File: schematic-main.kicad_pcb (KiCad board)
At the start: 2 copper layers, 87 x 72.4 mm, 73 parts, among them J1 Conn_01x02, J2 Conn_01x03, J3 Conn_01x02, J6 Conn_01x04, P1 USB_C_Plug_USB2.0, U1 LM76202-Q1, U2 TPS62933, U3 USBLC6-2P6, U4 ESP32-S3FN8, U5 SN65HVD232, U6 PC817, U7 PC817, Y1 Crystal_GND24

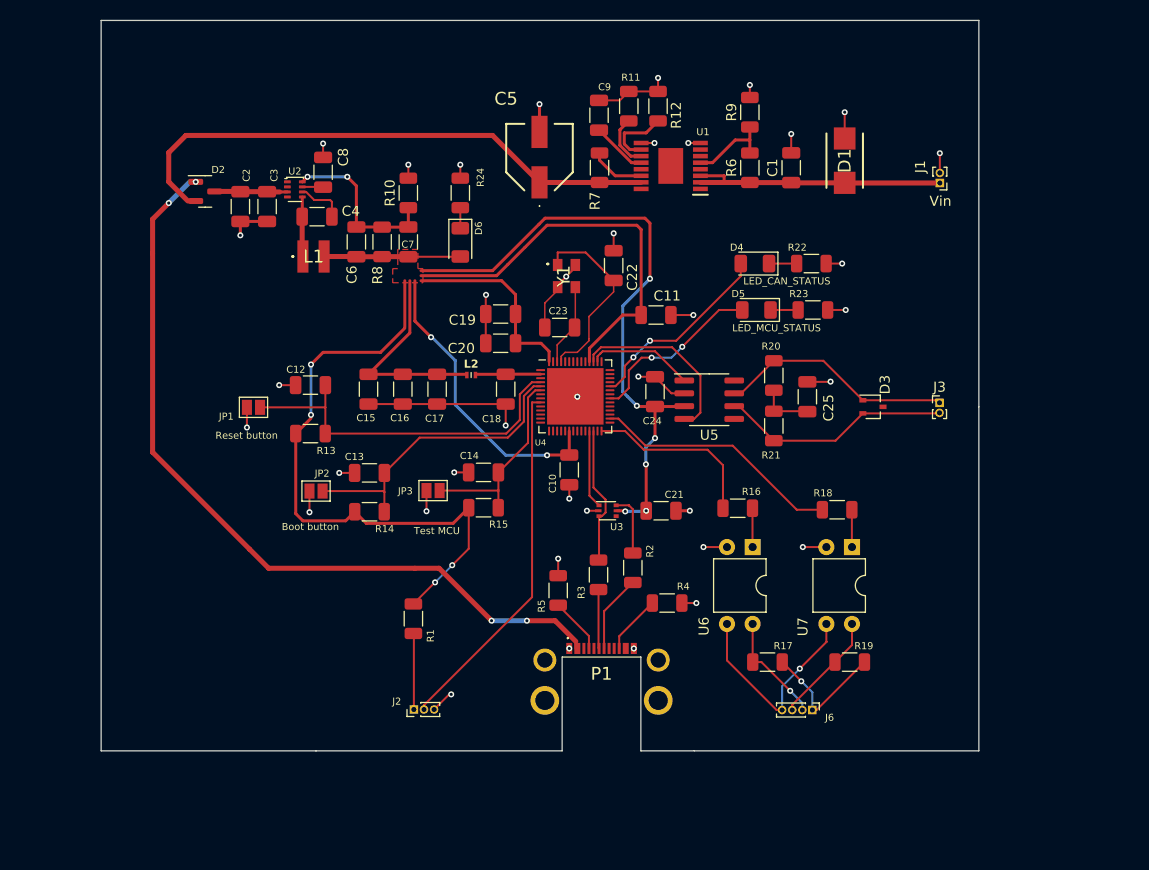
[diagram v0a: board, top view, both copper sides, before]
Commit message: Add Molex, change of layout for CAN and Optocouplers
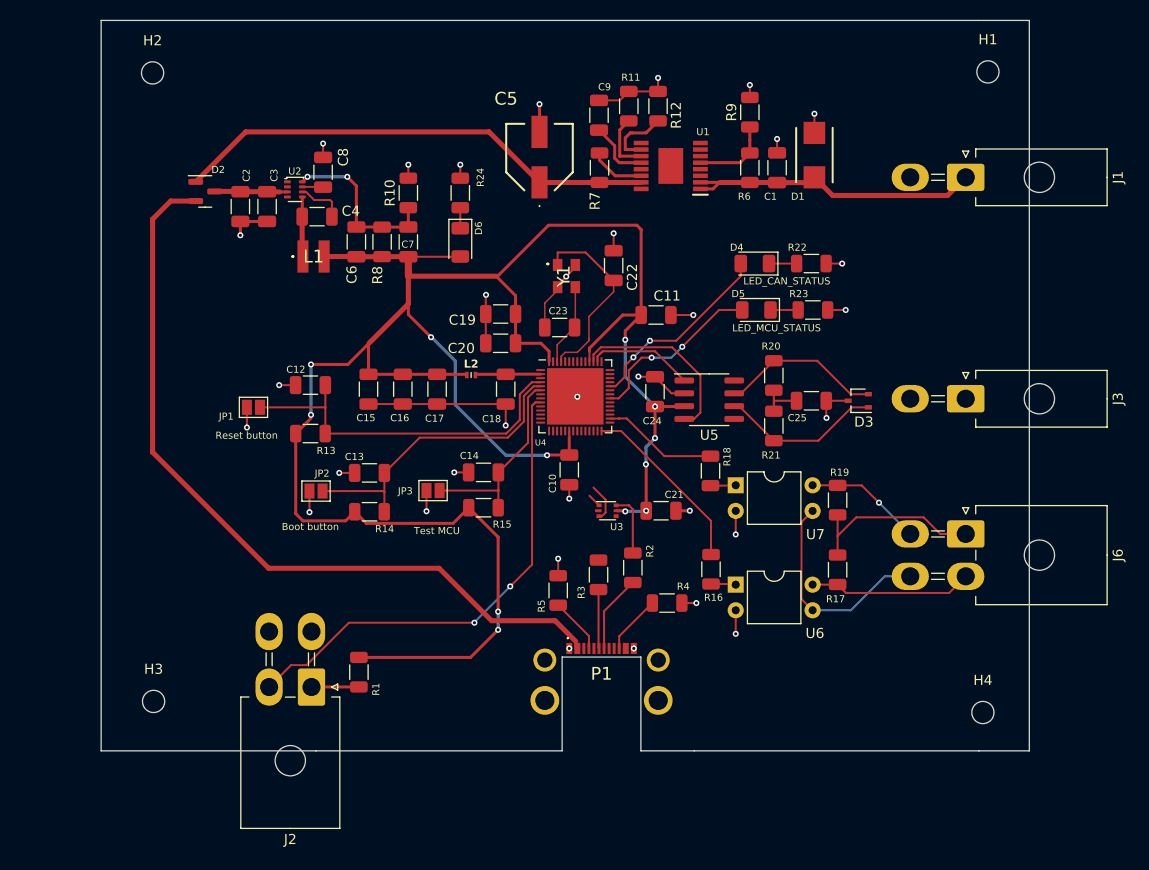
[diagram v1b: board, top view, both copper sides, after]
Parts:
- added H1: MountingHole, MountingHole:MountingHole_2.2mm_M2, F.Cu at (141.9, 56.8)
- added H2: MountingHole, MountingHole:MountingHole_2.2mm_M2, F.Cu at (59.1, 56.9)
- added H3: MountingHole, MountingHole:MountingHole_2.2mm_M2, F.Cu at (59.2, 119.2)
- added H4: MountingHole, MountingHole:MountingHole_2.2mm_M2, F.Cu at (141.4, 120.3)
- J1, J3: footprint Connector_PinHeader_1.00mm:PinHeader_1x02_P1.00mm_Vertical -> Connector_Molex:Molex_Mini-Fit_Jr_5569-02A2_2x01_P4.20mm_Horizontal
- J2: footprint Connector_PinHeader_1.00mm:PinHeader_1x03_P1.00mm_Vertical -> Connector_Molex:Molex_Mini-Fit_Jr_5569-04A2_2x02_P4.20mm_Horizontal
- J6: footprint Connector_PinHeader_1.00mm:PinHeader_1x04_P1.00mm_Vertical -> Connector_Molex:Molex_Mini-Fit_Jr_5569-04A2_2x02_P4.20mm_Horizontal
- moved J6 23.1 mm to (139.7, 102.6)
- moved R19 16.1 mm to (127.0, 99.2), turned to 90 degrees
- moved R18 13.1 mm to (114.4, 96.3), turned to -90 degrees
- moved U7 13.1 mm to (116.9, 97.8), turned to 0 degrees
- moved R17 11.5 mm to (127.0, 106.2), turned to -90 degrees
- moved J2 10.4 mm to (74.8, 117.8), turned to 180 degrees
- moved R1 7.57 mm to (79.5, 116.3)
- moved R16 6.60 mm to (114.5, 106.1), turned to -90 degrees
- moved U6 4.08 mm to (116.9, 107.6), turned to 0 degrees
- moved D1 3.05 mm to (124.7, 65.0)
- moved J3 2.63 mm to (139.7, 89.2), turned to -90 degrees
- moved J1 2.63 mm to (139.7, 67.2), turned to -90 degrees
- moved D3 1.57 mm to (129.1, 89.4), turned to 180 degrees
- moved C1 1.40 mm to (121.0, 66.3)
- moved C25 0.57 mm to (124.4, 89.4), turned to 0 degrees
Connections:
- D2 pad 1: /VBUS -> /Power /Vreg
- D2 pad 2: /Power /Vreg -> /VBUS
- D3 pad 1: /IO/CANH -> /IO/CANL
- D3 pad 2: /IO/CANL -> /IO/CANH
- U1 pad 2: /Power /Vin -> (no net)
- U1 pad 3: /Power /Vin -> (no net)
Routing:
- net +3.3V: track 249.1 -> 215.4 mm
- net /IO/MOTOR_ON_OFF_MCU: track 24.8 -> 11.5 mm
- net /MCU/SPEED_OUTPUT: track 35.7 -> 47.9 mm, vias 0 -> 2
- net /MCU/USB_D+: track 13.7 -> 3.84 mm
- net /Power /Vreg: track 55.8 -> 48.3 mm
- net /IO/CANH: track 23.4 -> 16.0 mm
- net /IO/CANL: track 22.9 -> 16.1 mm
- net /MCU/USB_D-: track 13.9 -> 7.50 mm
- net /PWM_MOTOR: track 11.1 -> 16.2 mm, vias 1 -> 0
- net GND: track 93.9 -> 88.9 mm, vias 36 -> 33
- net /IO/5V_MOTOR: track 13.1 -> 18.1 mm, vias 1 -> 0
- net /Power /Vin: track 26.8 -> 30.3 mm
- net Net-(J2-Pin_1): track 7.56 -> 4.71 mm
- net (no net): track 2.53 -> 0.00 mm, vias 2 -> 0
- net Net-(R18-Pad2): track 3.71 -> 2.52 mm
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- removed copper zone on F.Cu, net +3.3V
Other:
- board size 87 x 72.4 mm -> 92 x 72.4 mm
- board text removed: "Vin"

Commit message: Changing footprints for capacitors C >= 10 uF
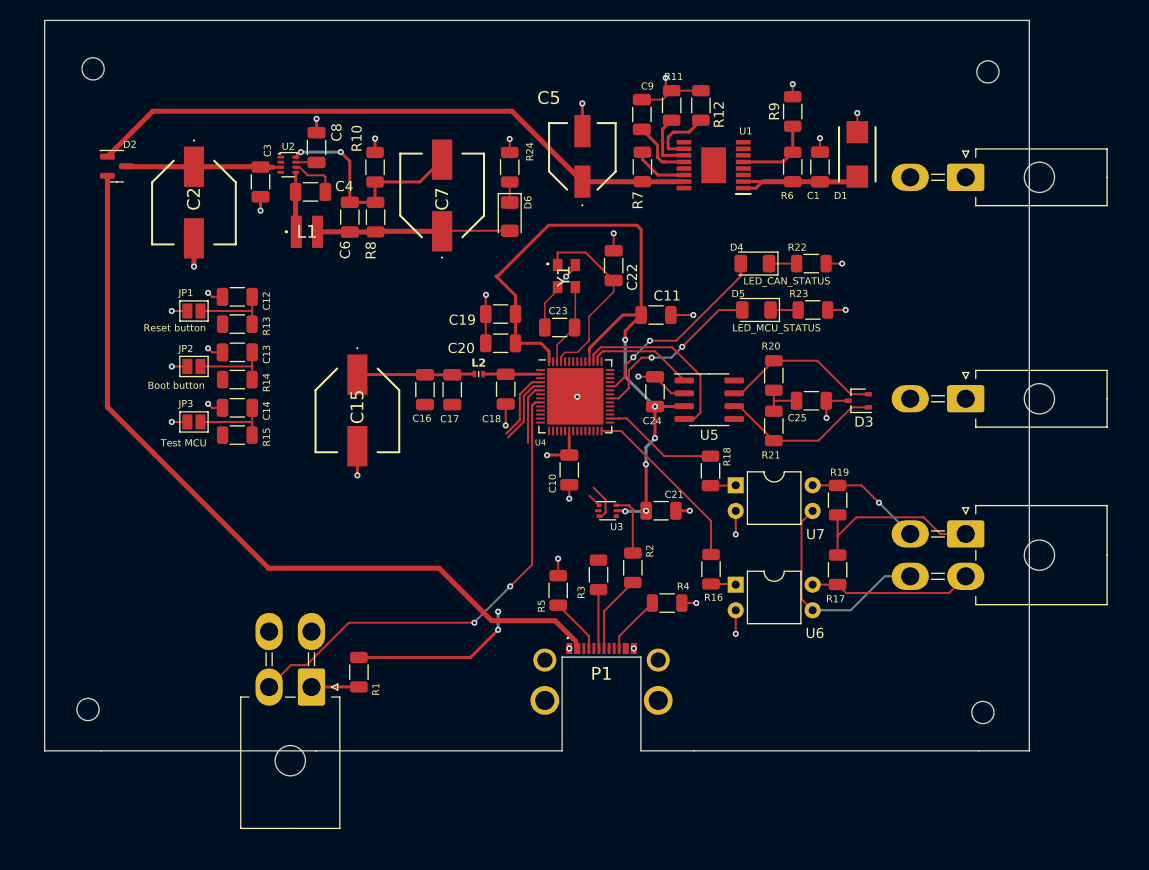
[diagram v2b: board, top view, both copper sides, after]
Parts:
- C15, C2, C7: footprint Capacitor_SMD:C_1206_3216Metric -> Capacitor_Tantalum_SMD:EEHZT1E331UP
- moved R15 25.4 mm to (67.5, 92.8)
- moved C14 25.2 mm to (67.5, 90.1)
- moved JP3 24.7 mm to (63.2, 91.5)
- moved R14 18.5 mm to (67.5, 87.3)
- moved C13 17.7 mm to (67.5, 84.6)
- moved JP2 17.3 mm to (63.2, 86.0)
- moved R13 13.0 mm to (67.5, 81.8)
- moved C12 11.4 mm to (67.5, 79.1)
- moved JP1 11.2 mm to (63.2, 80.5)
- moved D2 9.10 mm to (55.6, 66.2)
- moved H3 6.55 mm to (52.7, 120.0)
- moved H2 5.91 mm to (53.2, 56.5)
- moved C7 5.69 mm to (87.8, 69.0)
- moved D6 5.52 mm to (94.5, 71.2)
- moved R24 5.52 mm to (94.5, 66.2)
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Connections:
- U1 pad 15: /Power /Vreg -> (no net)
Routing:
- net +3.3V: track 215.4 -> 124.9 mm, vias 12 -> 9
- net /MCU/RESET: track 36.2 -> 14.8 mm
- net /Power /Vin: track 30.3 -> 13.8 mm
- net /MCU/BOOT: track 30.6 -> 14.7 mm
- net /Power /Vreg: track 48.3 -> 61.9 mm
- net GND: track 88.9 -> 77.1 mm, vias 33 -> 35
- net Net-(U2-VIN): track 7.27 -> 15.4 mm
- net /MCU/MCU_TEST: track 19.5 -> 13.8 mm
- net Net-(U2-FB): track 17.1 -> 22.2 mm
- net /VBUS: track 78.5 -> 79.9 mm
- net VDD3P3: track 6.78 -> 6.01 mm
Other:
- board size 92 x 72.4 mm -> 97.6 x 72.4 mm

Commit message: Adding library and fixing errors related to the ideal diode
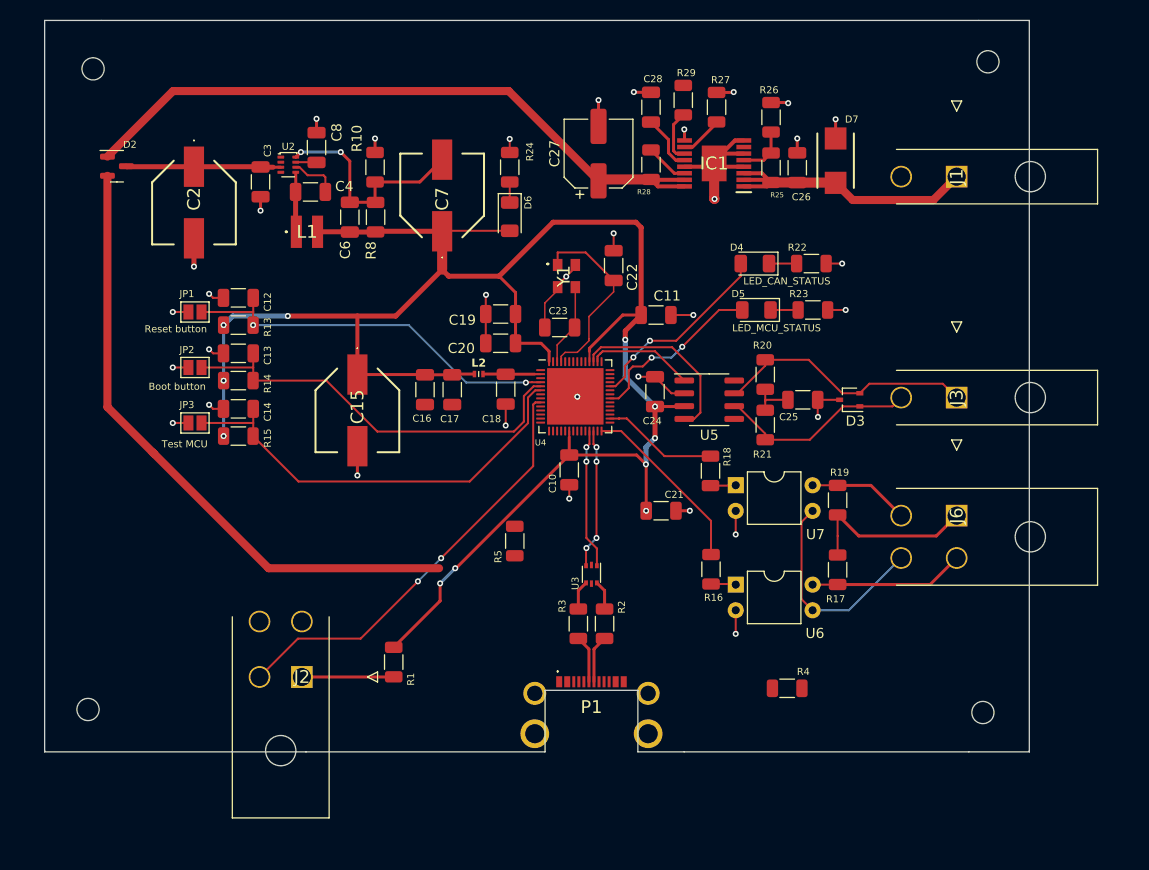
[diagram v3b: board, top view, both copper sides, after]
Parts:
- removed C1: 1u, Capacitor_SMD:C_1206_3216Metric
- removed C5: 47u, Capacitor_Tantalum_SMD:EEE0JA331XP
- removed C9: 2n7, Capacitor_SMD:C_1206_3216Metric
- removed D1: TPSMC30CA, Diode_SMD:DIONM5436X244N
- removed R11: 56k, Resistor_SMD:R_1206_3216Metric
- removed R12, R7: 100k, Resistor_SMD:R_1206_3216Metric
- removed R6: 180k, Resistor_SMD:R_1206_3216Metric
- removed R9: 12k, Resistor_SMD:R_1206_3216Metric
- removed U1: LM76202-Q1, Diode_SMD:SOP65P640X120-17N
- added C26: 1u, Capacitor_SMD:C_1206_3216Metric, F.Cu at (123.0, 66.3)
- added C27: 47u, Capacitor_SMD:CP_Elec_6.3x7.7, F.Cu at (103.3, 64.9)
- added C28: 2n7, Capacitor_SMD:C_1206_3216Metric, F.Cu at (108.5, 60.3)
- added D7: TPSMC30CA, Diode_SMD:DIONM5436X244N, F.Cu at (126.8, 65.6)
- added IC1: LM76202QPWPRQ1, Diode_SMD:SOP65P640X120-17N, F.Cu at (114.8, 65.9)
- added R25: 180k, Resistor_SMD:R_1206_3216Metric, F.Cu at (120.4, 66.3)
- added R26: 12k, Resistor_SMD:R_1206_3216Metric, F.Cu at (120.4, 61.3)
- added R27: 100k, Resistor_SMD:R_1206_3216Metric, F.Cu at (115.0, 60.3)
- added R28: 100k, Resistor_SMD:R_1206_3216Metric, F.Cu at (108.5, 66.0)
- added R29: 56k, Resistor_SMD:R_1206_3216Metric, F.Cu at (111.7, 59.6)
- J1, J3: footprint Connector_Molex:Molex_Mini-Fit_Jr_5569-02A2_2x01_P4.20mm_Horizontal -> Connector_Molex:39-30-102Y
- J2, J6: footprint Connector_Molex:Molex_Mini-Fit_Jr_5569-04A2_2x02_P4.20mm_Horizontal -> Connector_Molex:39-30-104Y
- moved R4 14.6 mm to (122.0, 117.9)
- moved R5 6.52 mm to (95.0, 103.3)
- moved U3 6.50 mm to (102.6, 106.6), turned to -90 degrees
- moved R2 6.22 mm to (103.9, 111.5)
- moved R3 5.25 mm to (101.3, 111.5)
- moved R1 3.59 mm to (83.0, 115.3)
- moved P1 3.45 mm to (102.6, 120.1)
- moved J6 2.03 mm to (138.8, 100.8), turned to 90 degrees
- moved J2 1.38 mm to (73.9, 116.8), turned to 0 degrees
- moved H1 1.00 mm to (141.9, 55.8)
- moved J3 0.91 mm to (138.8, 89.1), turned to 90 degrees
- moved J1 0.90 mm to (138.8, 67.2), turned to 90 degrees
- moved D3 0.86 mm to (128.2, 89.3)
- moved C25 0.86 mm to (123.5, 89.3)
- moved R20 0.86 mm to (119.8, 86.8)
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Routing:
- net +3.3V: track 124.9 -> 187.8 mm, vias 9 -> 11
- net /MCU/MCU_TEST: track 13.8 -> 43.4 mm
- net /MCU/BOOT: track 14.7 -> 41.8 mm
- net /MCU/RESET: track 14.8 -> 38.7 mm, vias 0 -> 2
- net /VBUS: track 79.9 -> 62.7 mm
- net /Power /Vin: track 13.8 -> 28.8 mm
- net /MCU/USB_D+: track 3.84 -> 16.8 mm, vias 0 -> 4
- net GND: track 77.1 -> 88.3 mm, vias 35 -> 34
- net /IO/CANH: track 16.0 -> 26.1 mm
- net /MCU/USB_D-: track 7.50 -> 16.8 mm, vias 0 -> 2
- net Net-(U1-OVP): track 7.87 -> 0.00 mm
- net Net-(U1-IMON): track 6.67 -> 0.00 mm
- net Net-(U1-dVdT): track 6.23 -> 0.00 mm
- net Net-(U1-ILIM): track 5.98 -> 0.00 mm
- net Net-(P1-VCONN): track 5.86 -> 0.00 mm
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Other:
- board size 97.6 x 72.4 mm -> 97.6 x 72.5 mm

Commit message: Adding filled areas and seting USB
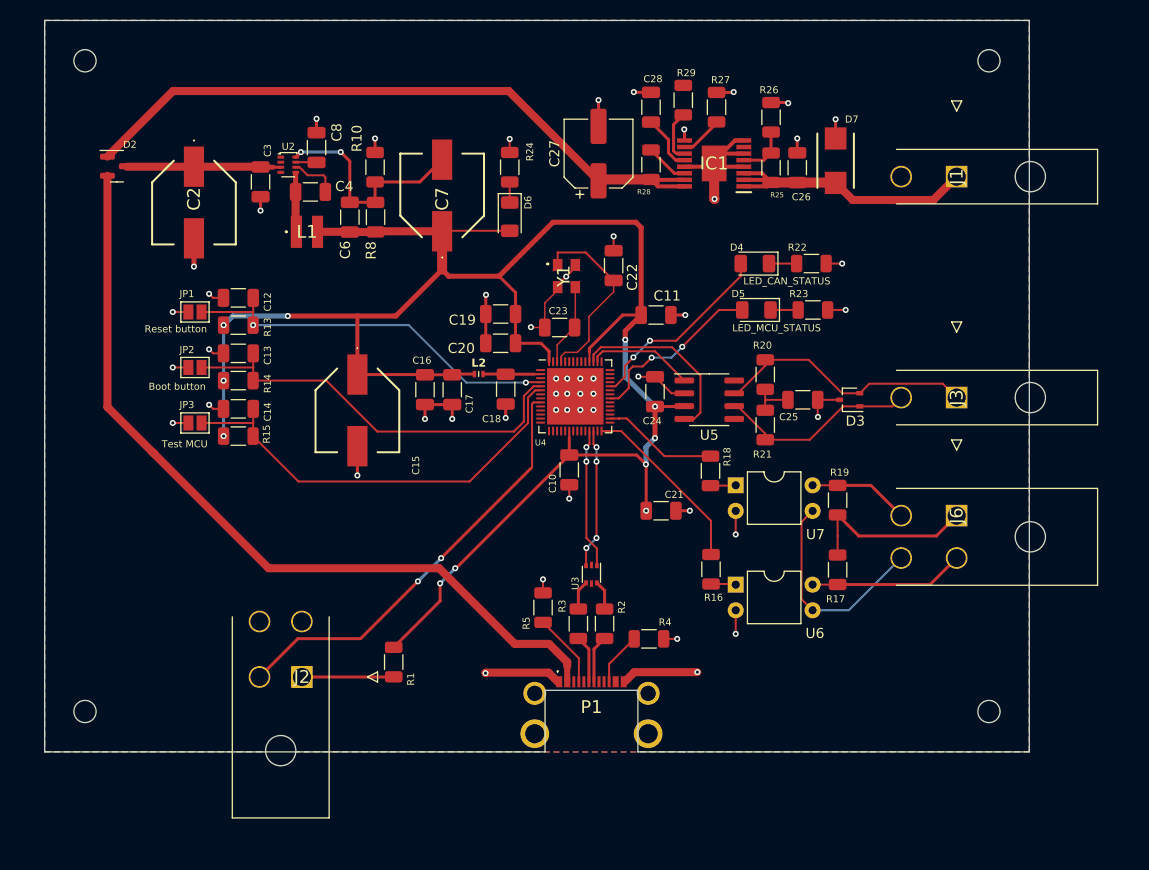
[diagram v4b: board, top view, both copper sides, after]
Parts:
- moved R4 14.5 mm to (108.3, 113.0)
- moved R5 7.17 mm to (97.8, 109.9)
- moved H2 1.13 mm to (52.4, 55.7)
- moved H4 0.61 mm to (142.0, 120.2)
- moved H3 0.36 mm to (52.4, 120.2)
- moved H1 0.14 mm to (142.0, 55.7)
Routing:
- net GND: track 88.3 -> 111.2 mm, vias 34 -> 52
- net /VBUS: track 62.7 -> 82.8 mm
- net Net-(P1-CC): track 0.00 -> 7.36 mm
- net Net-(P1-VCONN): track 0.00 -> 5.28 mm
- added copper zone on B.Cu, net GND
- added copper zone on F.Cu, net GND

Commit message: Changing placements of SolderJumper, CAN connector to 3 pins, traces 0,4
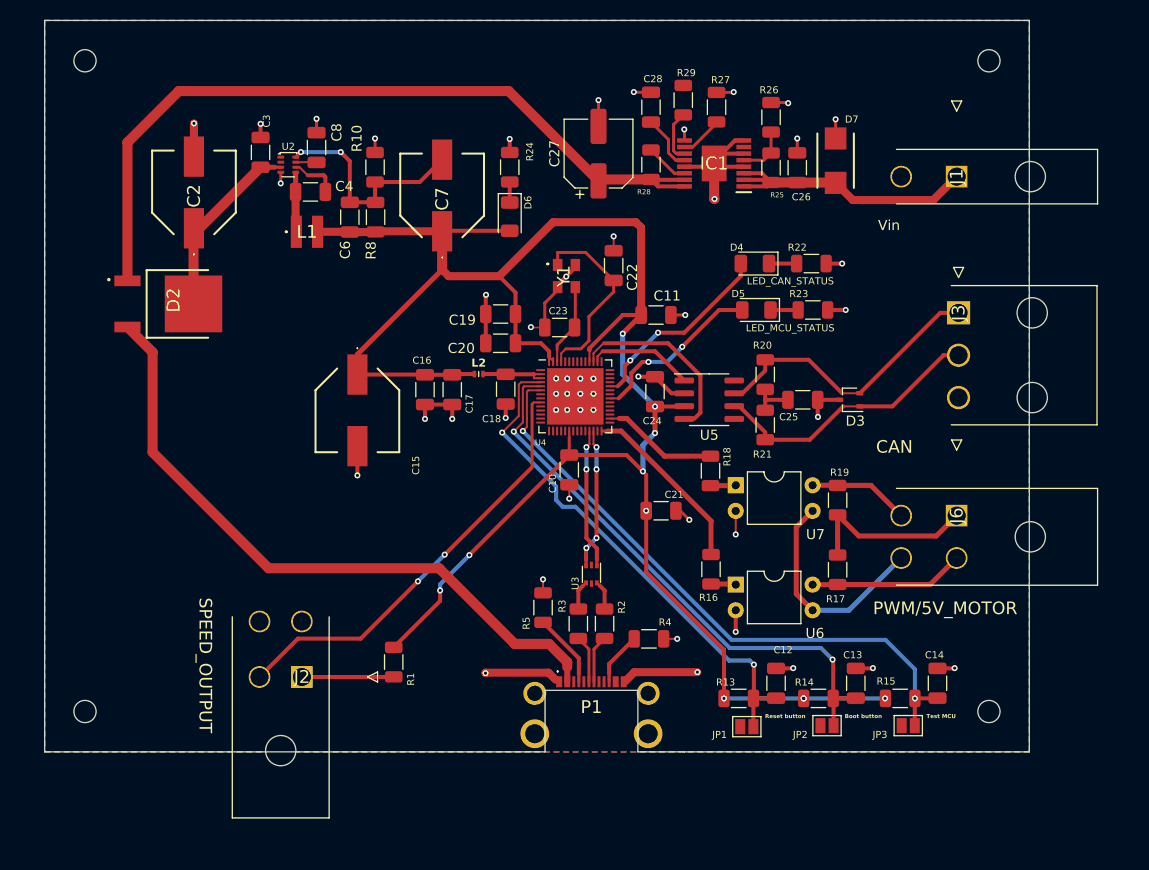
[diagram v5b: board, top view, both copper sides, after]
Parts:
- D2: footprint Package_TO_SOT_SMD:SOT-23 -> Diode_SMD:TO252__DPAK__1
- J3: value Conn_01x02 -> Conn_01x03_Pin; footprint Connector_Molex:39-30-102Y -> Connector_Molex:39303035
- moved JP3 76.8 mm to (134.0, 121.6)
- moved C14 74.4 mm to (136.9, 117.4), turned to 90 degrees
- moved JP2 72.0 mm to (126.0, 121.6)
- moved R15 70.6 mm to (133.2, 118.9)
- moved C13 69.4 mm to (128.8, 117.4), turned to 90 degrees
- moved JP1 68.4 mm to (118.0, 121.7)
- moved C12 65.6 mm to (120.9, 117.4), turned to 90 degrees
- moved R14 65.6 mm to (125.1, 118.9)
- moved R13 61.9 mm to (117.2, 118.9)
- moved D2 13.7 mm to (56.6, 79.8), turned to -90 degrees
- moved J3 8.40 mm to (139.0, 80.7)
- moved C3 2.92 mm to (69.8, 64.8), turned to 90 degrees
- moved C2 1.00 mm to (63.2, 68.8), turned to 90 degrees
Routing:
- net /MCU/MCU_TEST: track 43.4 -> 62.0 mm, vias 0 -> 2
- net /VBUS: track 82.8 -> 66.7 mm
- net /MCU/BOOT: track 41.8 -> 56.4 mm, vias 0 -> 2
- net /MCU/RESET: track 38.7 -> 51.4 mm
- net +3.3V: track 187.8 -> 199.7 mm
- net /Power /Vreg: track 67.3 -> 78.4 mm
- net /IO/CANL: track 20.0 -> 27.9 mm
- net Net-(U2-VIN): track 15.4 -> 18.7 mm
- net /IO/CANH: track 26.1 -> 29.3 mm
- net GND: track 111.2 -> 108.9 mm, vias 52 -> 50
- net VDD3P3: track 6.01 -> 7.08 mm
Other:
- board text added: "CAN"
- board text added: "PWM/5V_MOTOR"
- board text added: "SPEED_OUTPUT"
- board text added: "Vin"
